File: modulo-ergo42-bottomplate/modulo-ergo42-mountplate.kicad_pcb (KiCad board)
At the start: 2 copper layers, 137.2 x 80 mm, 14 parts

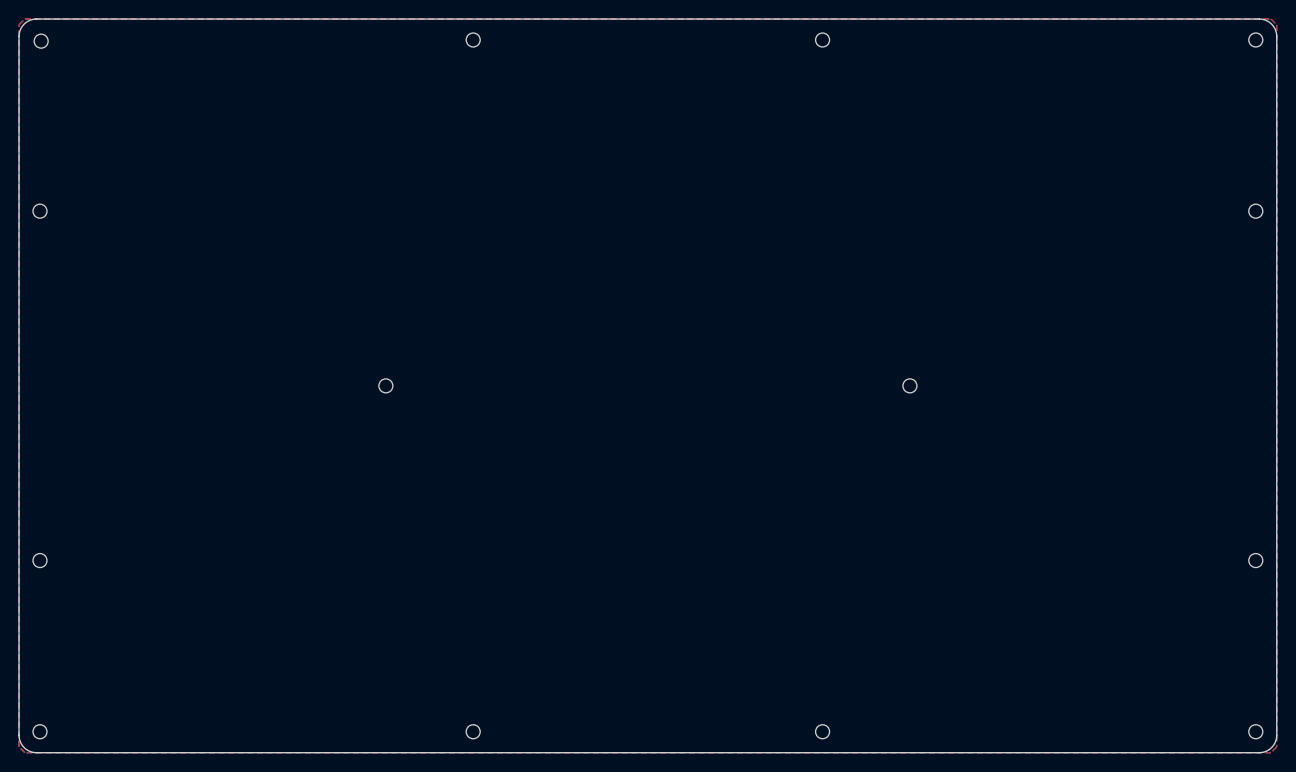
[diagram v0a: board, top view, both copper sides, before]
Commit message: Fix bottom plate screw hole
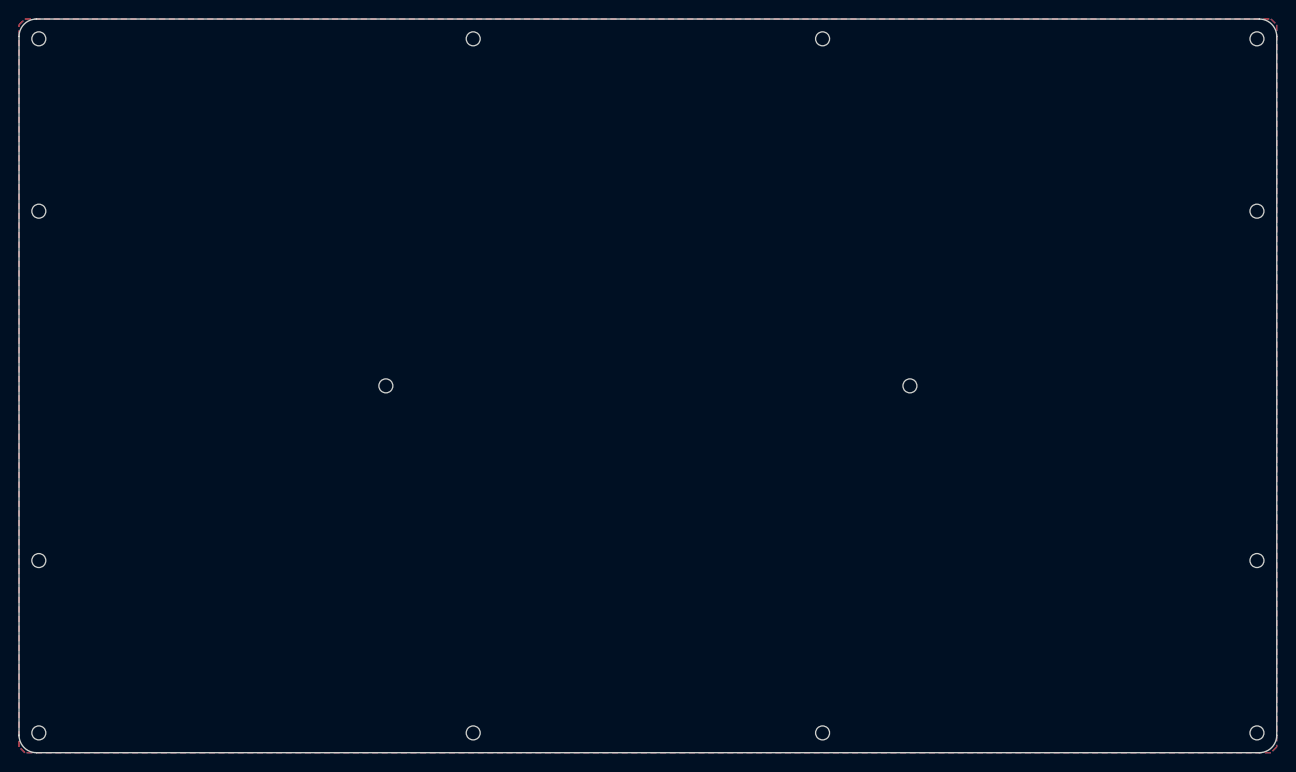
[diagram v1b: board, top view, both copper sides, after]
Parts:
- removed the ? at (56.9, 55.2)
- removed the ? at (142.2, 112.0)
- removed the ? at (189.5, 112.0)
- removed the ? at (189.5, 36.6)
- removed the ? at (56.9, 93.3)
- removed the ? at (189.5, 93.3)
- removed the ? at (189.5, 55.2)
- removed the ? at (142.2, 36.6)
- removed the ? at (57.0, 36.7)
- removed the ? at (56.9, 112.0)
- removed the ? at (104.1, 112.0)
- added ?: Screw_Hole, library:Screw_Hole, F.Cu at (56.8, 55.2)
- added ?: Screw_Hole, library:Screw_Hole, F.Cu at (142.2, 112.1)
- added ?: Screw_Hole, library:Screw_Hole, F.Cu at (189.6, 112.1)
- added ?: Screw_Hole, library:Screw_Hole, F.Cu at (189.6, 36.4)
- added ?: Screw_Hole, library:Screw_Hole, F.Cu at (56.8, 93.3)
- added ?: Screw_Hole, library:Screw_Hole, F.Cu at (189.6, 93.3)
- added ?: Screw_Hole, library:Screw_Hole, F.Cu at (189.6, 55.2)
- added ?: Screw_Hole, library:Screw_Hole, F.Cu at (142.2, 36.4)
- added ?: Screw_Hole, library:Screw_Hole, F.Cu at (56.8, 36.4)
- added ?: Screw_Hole, library:Screw_Hole, F.Cu at (56.8, 112.1)
- added ?: Screw_Hole, library:Screw_Hole, F.Cu at (104.1, 112.1)
- moved ? 0.13 mm to (104.1, 36.4)
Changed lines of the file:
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@@
   )
   (module library:Screw_Hole (layer F.Cu)
-    (at 56.896 55.245)
+    (at 56.769 55.245)
     (fp_text reference "" (at 0 1.905) (layer F.SilkS)
       (effects (font (size 1 1) (thickness 0.15)))
@@
   )
   (module library:Screw_Hole (layer F.Cu)
-    (at 56.896 93.345)
+    (at 56.769 93.345)
     (fp_text reference "" (at 0 1.905) (layer F.SilkS)
       (effects (font (size 1 1) (thickness 0.15)))
@@
   )
   (module library:Screw_Hole (layer F.Cu)
-    (at 189.484 93.345)
+    (at 189.611 93.345)
     (fp_text reference "" (at 0 1.905) (layer F.SilkS)
       (effects (font (size 1 1) (thickness 0.15)))
@@
   )
   (module library:Screw_Hole (layer F.Cu)
-    (at 189.484 55.245)
+    (at 189.611 55.245)
     (fp_text reference "" (at 0 1.905) (layer F.SilkS)
       (effects (font (size 1 1) (thickness 0.15)))
@@
   )
   (module library:Screw_Hole (layer F.Cu)
-    (at 142.24 36.576)
+    (at 142.24 36.449)
     (fp_text reference "" (at 0 1.905) (layer F.SilkS)
       (effects (font (size 1 1) (thickness 0.15)))
@@
   )
   (module library:Screw_Hole (layer F.Cu)
-    (at 104.14 36.576)
+    (at 104.14 36.449)
     (fp_text reference "" (at 0 1.905) (layer F.SilkS)
       (effects (font (size 1 1) (thickness 0.15)))
@@
   )
   (module library:Screw_Hole (layer F.Cu)
-    (at 57.023 36.703)
+    (at 56.769 36.449)
     (fp_text reference "" (at 0 1.905) (layer F.SilkS)
       (effects (font (size 1 1) (thickness 0.15)))
@@
   )
   (module library:Screw_Hole (layer F.Cu)
-    (at 56.896 112.014)
+    (at 56.769 112.141)
     (fp_text reference "" (at 0 1.905) (layer F.SilkS)
       (effects (font (size 1 1) (thickness 0.15)))
@@
   )
   (module library:Screw_Hole (layer F.Cu)
-    (at 104.14 112.014)
+    (at 104.14 112.141)
     (fp_text reference "" (at 0 1.905) (layer F.SilkS)
       (effects (font (size 1 1) (thickness 0.15)))
@@
   )
   (module library:Screw_Hole (layer F.Cu)
-    (at 142.24 112.014)
+    (at 142.24 112.141)
     (fp_text reference "" (at 0 1.905) (layer F.SilkS)
       (effects (font (size 1 1) (thickness 0.15)))
@@
   )
   (module library:Screw_Hole (layer F.Cu)
-    (at 189.484 112.014)
+    (at 189.611 112.141)
     (fp_text reference "" (at 0 1.905) (layer F.SilkS)
       (effects (font (size 1 1) (thickness 0.15)))
@@
   )
   (module library:Screw_Hole (layer F.Cu)
-    (at 189.484 36.576)
+    (at 189.611 36.449)
     (fp_text reference "" (at 0 1.905) (layer F.SilkS)
       (effects (font (size 1 1) (thickness 0.15)))
